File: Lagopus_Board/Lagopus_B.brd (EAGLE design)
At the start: 20.3 x 58.4 mm, 10 parts, among them J1 PTH, U1 TMP1021:1, U3 BME280

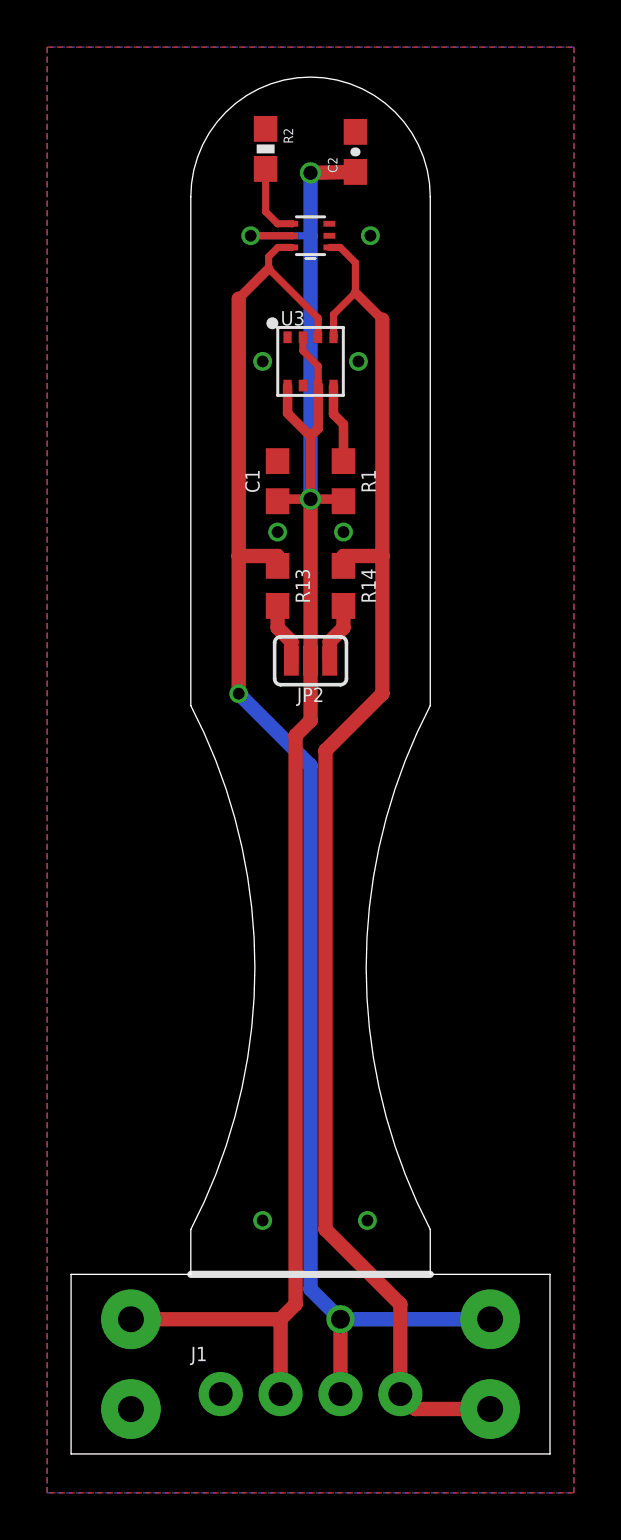
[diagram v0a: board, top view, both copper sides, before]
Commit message: Ordered Version 1.0 from Seeed
Lemming_SMD V1.0
Lagopus_A V1.0
Lagopus_B V1.0
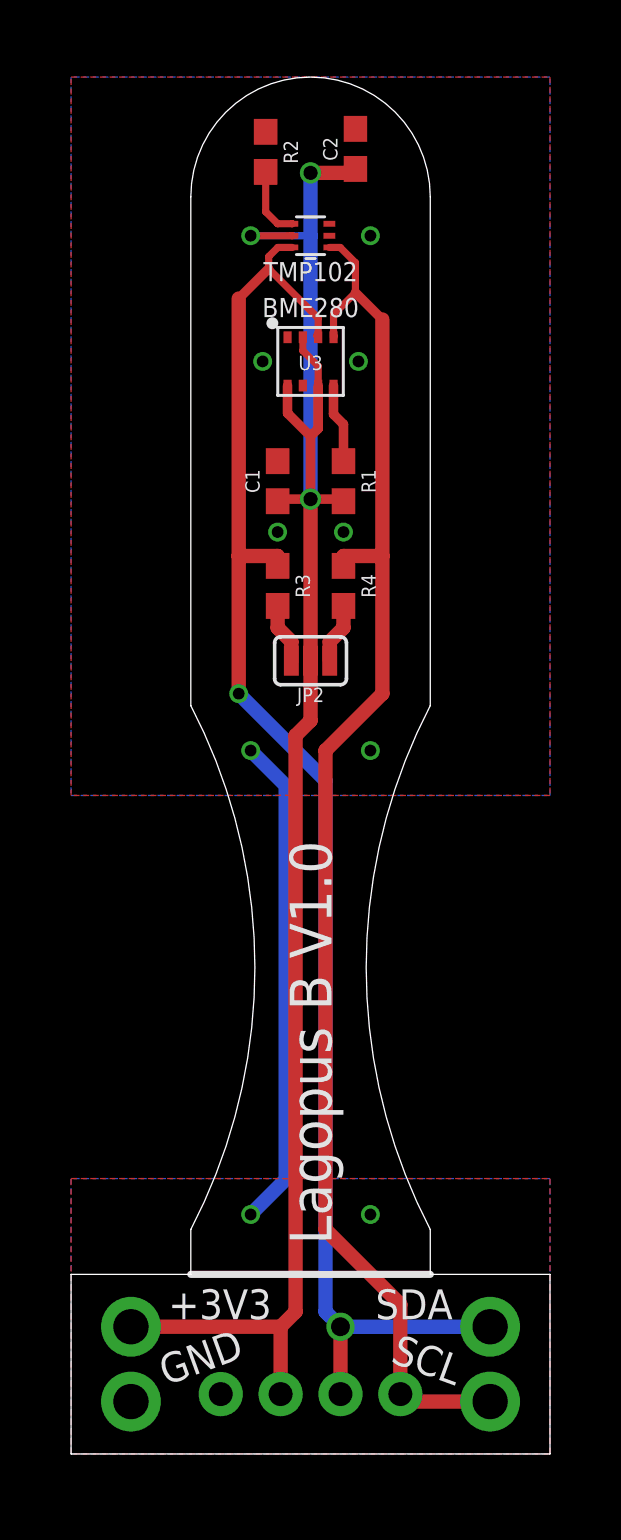
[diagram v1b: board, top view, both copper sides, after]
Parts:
- C2: device SparkFun-Capacitors:0603-CAP -> SparkFun-Capacitors:0603
- R2: value 10K -> 10k; device SparkFun-Resistors:0603-RES -> SparkFun-Resistors:0603
- moved C2 0.13 mm to (1.91, 47.8)
- moved R2 0.13 mm to (-1.91, 47.6)
- renumbered R13 to R3, R14 to R4
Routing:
- net GND: track 0.00 -> 21.0 mm, vias 8 -> 10
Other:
- board text added: "(C) 2018 john.hulth@geo.uio.no"
- board text added: "+3V3"
- board text added: "GND"
- board text added: "Lagopus B V1.0"
- board text added: "SCL"
- board text added: "SDA"
- board text added: "TMP102"
